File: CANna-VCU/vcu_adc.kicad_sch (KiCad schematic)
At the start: 38 parts, among them U4 TLV274

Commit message: first draft of full board
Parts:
- added C39, C40, C41, C42, C47: 100n, Capacitor_SMD:C_0402_1005Metric, symbol Device:C_Small
- added C43, C44, C45, C46: 1n, Capacitor_SMD:C_0402_1005Metric, symbol Device:C_Small
- added D10, D11, D12, D13: BZX84-C3V3, Package_TO_SOT_SMD:SOT-23, symbol Diode:BZX84Cxx
- added R38, R39, R40, R41: 100k, Resistor_SMD:R_0402_1005Metric, symbol Device:R_Small
- added R42, R43, R44, R45: 1k, Resistor_SMD:R_0402_1005Metric, symbol Device:R_Small
- added R46, R50, R54, R58: 75k, Resistor_SMD:R_0402_1005Metric, symbol Device:R_Small
- added R47, R48, R51, R52, R55, R56, R59, R60: 5.6k, Resistor_SMD:R_0402_1005Metric, symbol Device:R_Small
- added R49, R53, R57, R61: 1.8k, Resistor_SMD:R_0402_1005Metric, symbol Device:R_Small
- added U8: TLV274, Package_SO:SOIC-14_3.9x8.7mm_P1.27mm, symbol Amplifier_Operational:TLC274
- C31: renamed from C4; footprint Capacitor_SMD:C_0805_2012Metric_Pad1.18x1.45mm_HandSolder -> Capacitor_SMD:C_0402_1005Metric
- C32: renamed from C5; footprint Capacitor_SMD:C_0805_2012Metric_Pad1.18x1.45mm_HandSolder -> Capacitor_SMD:C_0402_1005Metric
- C33: renamed from C6; footprint Capacitor_SMD:C_0805_2012Metric_Pad1.18x1.45mm_HandSolder -> Capacitor_SMD:C_0402_1005Metric
- C34: renamed from C7; footprint Capacitor_SMD:C_0805_2012Metric_Pad1.18x1.45mm_HandSolder -> Capacitor_SMD:C_0402_1005Metric
- C35: renamed from C8; footprint Capacitor_SMD:C_0805_2012Metric_Pad1.18x1.45mm_HandSolder -> Capacitor_SMD:C_0402_1005Metric
- C36: renamed from C9; footprint Capacitor_SMD:C_0805_2012Metric_Pad1.18x1.45mm_HandSolder -> Capacitor_SMD:C_0402_1005Metric
- C37: renamed from C10; footprint Capacitor_SMD:C_0805_2012Metric_Pad1.18x1.45mm_HandSolder -> Capacitor_SMD:C_0402_1005Metric
- C38: renamed from C11; footprint Capacitor_SMD:C_0805_2012Metric_Pad1.18x1.45mm_HandSolder -> Capacitor_SMD:C_0402_1005Metric
- C48: renamed from C12; footprint Capacitor_SMD:C_0805_2012Metric_Pad1.18x1.45mm_HandSolder -> Capacitor_SMD:C_0402_1005Metric
- R14: renamed from R12; footprint Resistor_SMD:R_0805_2012Metric_Pad1.20x1.40mm_HandSolder -> Resistor_SMD:R_0402_1005Metric
- R15: renamed from R13; footprint Resistor_SMD:R_0805_2012Metric_Pad1.20x1.40mm_HandSolder -> Resistor_SMD:R_0402_1005Metric
- R16: renamed from R14; footprint Resistor_SMD:R_0805_2012Metric_Pad1.20x1.40mm_HandSolder -> Resistor_SMD:R_0402_1005Metric
- R17: renamed from R15; footprint Resistor_SMD:R_0805_2012Metric_Pad1.20x1.40mm_HandSolder -> Resistor_SMD:R_0402_1005Metric
- R18: renamed from R16; footprint Resistor_SMD:R_0805_2012Metric_Pad1.20x1.40mm_HandSolder -> Resistor_SMD:R_0402_1005Metric
- R19: renamed from R17; footprint Resistor_SMD:R_0805_2012Metric_Pad1.20x1.40mm_HandSolder -> Resistor_SMD:R_0402_1005Metric
- R20: renamed from R18; footprint Resistor_SMD:R_0805_2012Metric_Pad1.20x1.40mm_HandSolder -> Resistor_SMD:R_0402_1005Metric
- R21: renamed from R19; footprint Resistor_SMD:R_0805_2012Metric_Pad1.20x1.40mm_HandSolder -> Resistor_SMD:R_0402_1005Metric
- R22: renamed from R20; footprint Resistor_SMD:R_0805_2012Metric_Pad1.20x1.40mm_HandSolder -> Resistor_SMD:R_0402_1005Metric
- R23: renamed from R21; footprint Resistor_SMD:R_0805_2012Metric_Pad1.20x1.40mm_HandSolder -> Resistor_SMD:R_0402_1005Metric
- R24: renamed from R22; footprint Resistor_SMD:R_0805_2012Metric_Pad1.20x1.40mm_HandSolder -> Resistor_SMD:R_0402_1005Metric
- R25: renamed from R23; footprint Resistor_SMD:R_0805_2012Metric_Pad1.20x1.40mm_HandSolder -> Resistor_SMD:R_0402_1005Metric
- R26: renamed from R24; footprint Resistor_SMD:R_0805_2012Metric_Pad1.20x1.40mm_HandSolder -> Resistor_SMD:R_0402_1005Metric
- R27: renamed from R25; footprint Resistor_SMD:R_0805_2012Metric_Pad1.20x1.40mm_HandSolder -> Resistor_SMD:R_0402_1005Metric
- R28: renamed from R26; footprint Resistor_SMD:R_0805_2012Metric_Pad1.20x1.40mm_HandSolder -> Resistor_SMD:R_0402_1005Metric
- R29: renamed from R27; footprint Resistor_SMD:R_0805_2012Metric_Pad1.20x1.40mm_HandSolder -> Resistor_SMD:R_0402_1005Metric
- R30: renamed from R28; footprint Resistor_SMD:R_0805_2012Metric_Pad1.20x1.40mm_HandSolder -> Resistor_SMD:R_0402_1005Metric
- R31: renamed from R29; footprint Resistor_SMD:R_0805_2012Metric_Pad1.20x1.40mm_HandSolder -> Resistor_SMD:R_0402_1005Metric
- R32: renamed from R30; footprint Resistor_SMD:R_0805_2012Metric_Pad1.20x1.40mm_HandSolder -> Resistor_SMD:R_0402_1005Metric
- R33: renamed from R31; footprint Resistor_SMD:R_0805_2012Metric_Pad1.20x1.40mm_HandSolder -> Resistor_SMD:R_0402_1005Metric
- R34: renamed from R32; footprint Resistor_SMD:R_0805_2012Metric_Pad1.20x1.40mm_HandSolder -> Resistor_SMD:R_0402_1005Metric
- R35: renamed from R33; footprint Resistor_SMD:R_0805_2012Metric_Pad1.20x1.40mm_HandSolder -> Resistor_SMD:R_0402_1005Metric
- R36: renamed from R34; footprint Resistor_SMD:R_0805_2012Metric_Pad1.20x1.40mm_HandSolder -> Resistor_SMD:R_0402_1005Metric
- R37: renamed from R35; footprint Resistor_SMD:R_0805_2012Metric_Pad1.20x1.40mm_HandSolder -> Resistor_SMD:R_0402_1005Metric
- renumbered D1 to D6, D2 to D7, D3 to D8, D4 to D9, U4 to U7
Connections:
- net +12V: now also C47.2, U8.4 (V+)
- net APPS_1_IN: now also R41.1, R45.1
- net APPS_1_OUT: now also C44.2, D13.3 (K), R59.2, R60.1
- net APPS_2_IN: now also R40.1, R44.1
- net APPS_2_OUT: now also C43.2, D12.3 (K), R55.2, R56.1
- net BPS_IN: now also R38.1, R42.1
- net BPS_OUT: now also C45.2, D10.3 (K), R47.2, R48.1
- net GND: now also C39.1, C40.1, C41.1, C42.1, C43.1, C44.1, C45.1, C46.1, C47.1, D10.1 (A), D11.1 (A), D12.1 (A), D13.1 (A), R38.2, R39.2, R40.2, R41.2, R49.2, R53.2, R57.2, R61.2, U8.11 (V-)
- net SAGL_IN: now also R39.1, R43.1
- net SAGL_OUT: now also C46.2, D11.3 (K), R51.2, R52.1
- new net: R56.2, R57.1
- new net: R58.2, R59.1
- new net: C42.2, R45.2, U8.10 (+)
- new net: C41.2, R44.2, U8.12 (+)
- new net: R48.2, R49.1
- new net: C40.2, R43.2, U8.3 (+)
- new net: R50.1, U8.1, U8.2 (-)
- new net: R54.1, U8.13 (-), U8.14
- new net: R54.2, R55.1
- new net: R46.2, R47.1
- new net: R50.2, R51.1
- new net: C39.2, R42.2, U8.5 (+)
- new net: R46.1, U8.6 (-), U8.7
- new net: R52.2, R53.1
- new net: R60.2, R61.1
- new net: R58.1, U8.8, U8.9 (-)
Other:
- moved on the sheet: C48, U7E

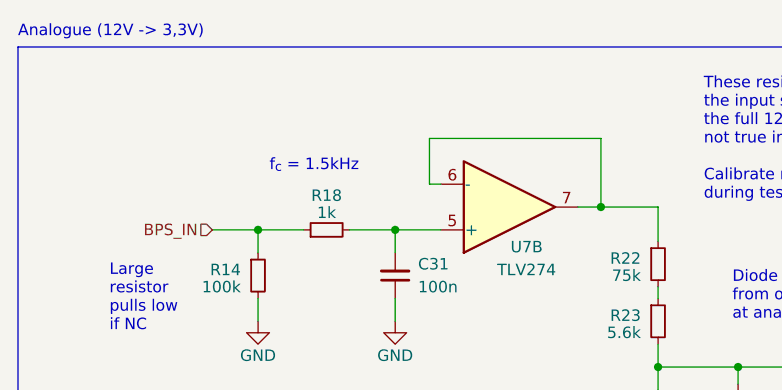
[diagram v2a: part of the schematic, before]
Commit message: added power managment bits
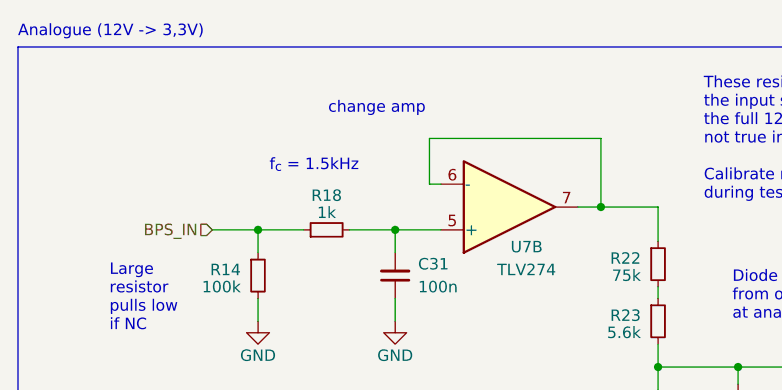
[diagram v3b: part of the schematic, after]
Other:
- note added: "change amp"
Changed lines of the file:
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@@
+		)
+	)
+	(text "change amp"
+		(exclude_from_sim no)
+		(at 74.168 39.878 0)
+		(effects
+			(font
+				(size 1.27 1.27)
+			)
 		)
 	)
